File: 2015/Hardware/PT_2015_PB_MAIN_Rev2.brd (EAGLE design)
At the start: 142.2 x 170.8 mm, 135 parts, among them Q1 Q_ACS711LC, Q11 Q_IRFS7437PbF, Q12 2N7002, Q14 Q_IRFS7437PbF, Q16 Q_IRFS7437PbF, Q18 Q_FDT86102LZ, Q20 Q_IRFS7437PbF, Q4 Q_ACS711LC, Q5 Q_ACS711LC, Q6 Q_IRFS7437PbF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

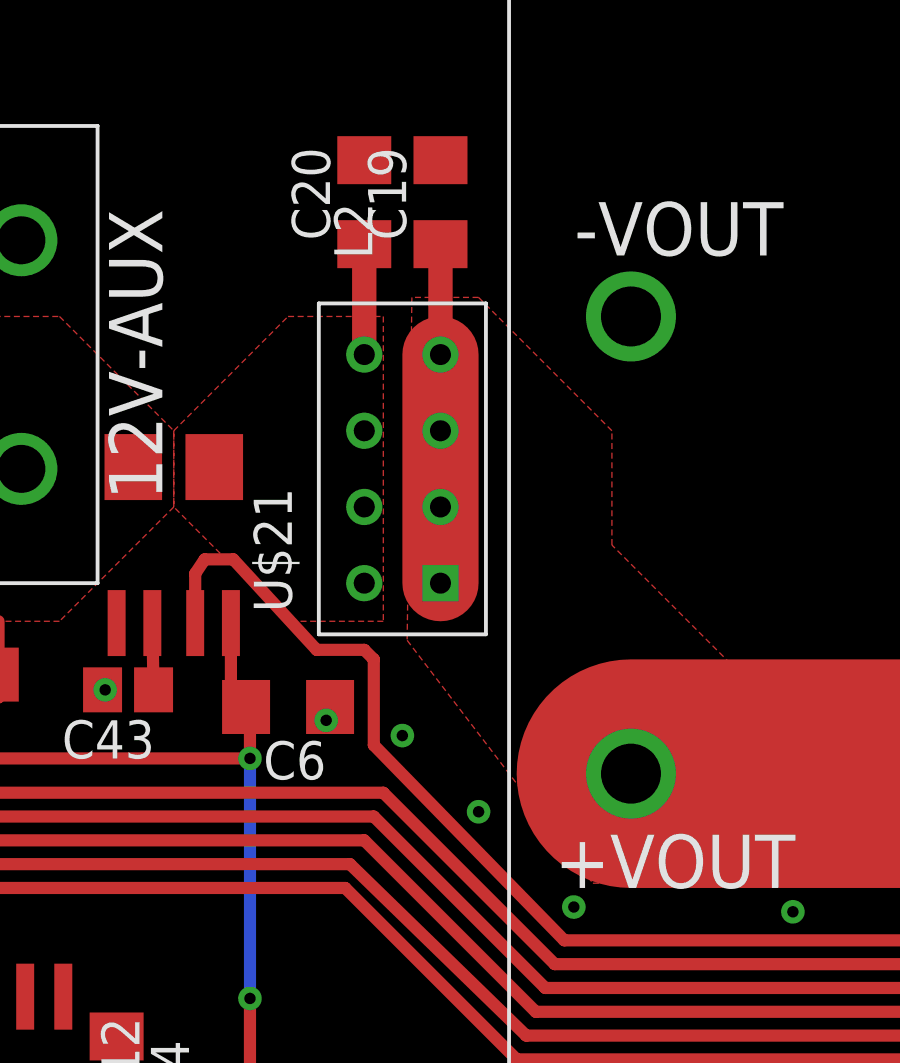
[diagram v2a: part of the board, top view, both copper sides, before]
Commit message: Removed ferrite bede on 12V non-critical output
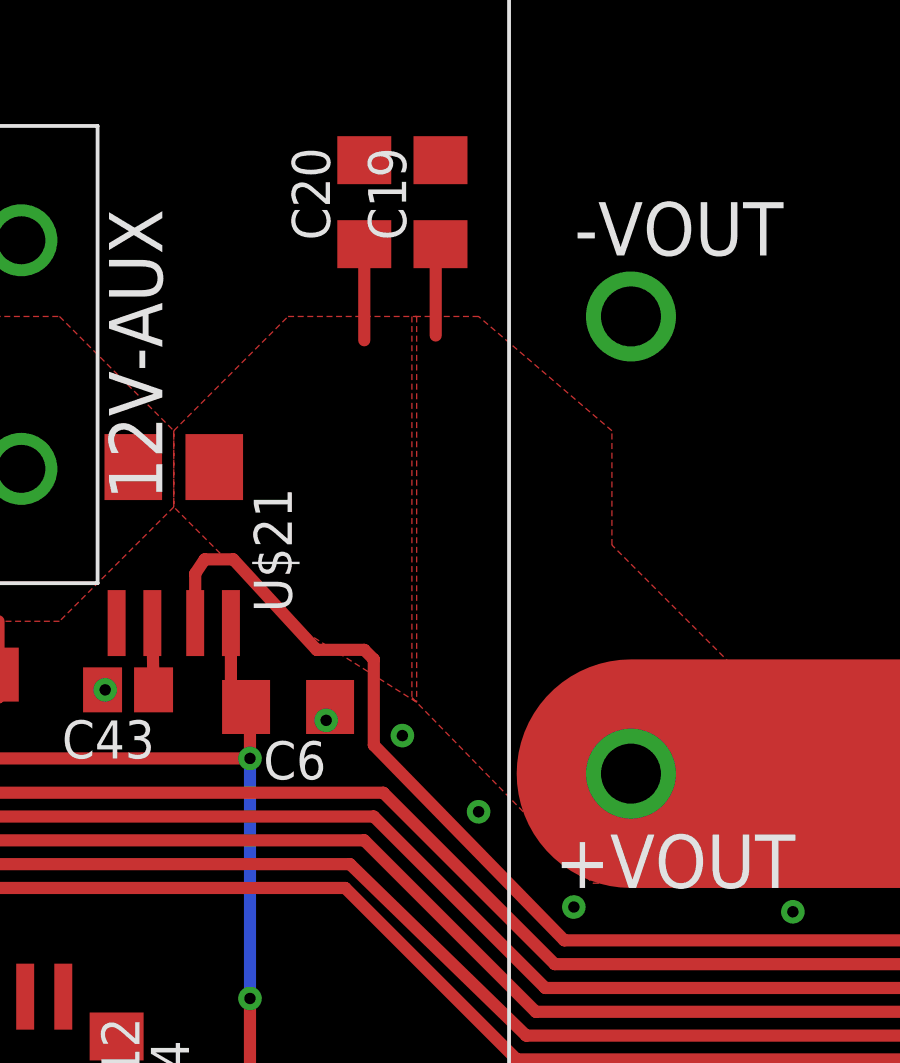
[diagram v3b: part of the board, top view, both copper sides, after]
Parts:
- removed L2: L_29F0429, MRDT-2014-All:L_29F0429
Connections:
- removed net N$11: C20.1, L2.5, L2.6, L2.7, L2.8, U$21.1
- net N$7: now also C20.1, U$21.1; no longer L2.1, L2.2, L2.3, L2.4
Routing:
- net N$7: track 88.5 -> 83.6 mm
- net N$11: track 3.68 -> 0.00 mm
- removed copper zone on layer 1, net N$11
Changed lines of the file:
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@@
 <attribute name="NAME" x="81.01" y="79.36" size="1.27" layer="25" rot="R270"/>
-</element>
-<element name="L2" library="MRDT-2014-All" package="L_29F0429" value="L_29F0429" x="24.13" y="146.05" smashed="yes" rot="R90">
-<attribute name="NAME" x="23.13" y="153.05" size="1.27" layer="25" rot="R90"/>
 </element>
 <element name="U$2" library="MRDT-2014-All" package="SOD-323" value="D_SD12T1G" x="132.08" y="99.06"/>
@@
 <contactref element="PALPATINE-12V" pad="8"/>
 <contactref element="SIDEOUS-12V" pad="8"/>
-<contactref element="L2" pad="4"/>
-<contactref element="L2" pad="1"/>
-<contactref element="L2" pad="2"/>
-<contactref element="L2" pad="3"/>
 <contactref element="C19" pad="1"/>
-<wire x1="25.4" y1="149.86" x2="25.4" y2="153.54" width="0.8128" layer="1"/>
-<wire x1="25.4" y1="149.86" x2="25.4" y2="142.24" width="2.54" layer="1"/>
 <wire x1="31.75" y1="135.89" x2="57.785" y2="135.89" width="7.62" layer="1"/>
 <wire x1="57.785" y1="135.89" x2="80.01" y2="158.115" width="7.62" layer="1"/>
 <wire x1="80.01" y1="158.115" x2="99.695" y2="158.115" width="7.62" layer="1"/>
 <polygon width="0.4064" layer="1">
-<vertex x="26.67" y="151.765"/>
-<vertex x="24.4475" y="151.765"/>
-<vertex x="24.28875" y="140.335"/>
+<vertex x="26.67" y="151.13"/>
+<vertex x="24.4475" y="151.13"/>
+<vertex x="24.4475" y="138.43"/>
 <vertex x="30.48" y="132.23875"/>
 <vertex x="36.195" y="132.23875"/>
@@
 <vertex x="31.115" y="147.32"/>
 </polygon>
-</signal>
-<signal name="N$11">
-<contactref element="L2" pad="8"/>
-<contactref element="L2" pad="5"/>
-<contactref element="L2" pad="7"/>
-<contactref element="L2" pad="6"/>
 <contactref element="C20" pad="1"/>
 <contactref element="U$21" pad="1"/>
 <polygon width="0.4064" layer="1" thermals="no">
-<vertex x="23.495" y="151.13"/>
-<vertex x="23.495" y="140.97"/>
+<vertex x="24.60625" y="151.13"/>
+<vertex x="24.60625" y="138.27125"/>
 <vertex x="20.32" y="140.97"/>
 <vertex x="16.51" y="144.78"/>
@@
 <vertex x="20.32" y="151.13"/>
 </polygon>
-<wire x1="22.86" y1="153.54" x2="22.86" y2="149.86" width="0.8128" layer="1"/>
+<wire x1="22.86" y1="153.54" x2="22.86" y2="150.33625" width="0.4064" layer="1"/>
+<wire x1="25.4" y1="153.54" x2="25.24125" y2="153.54" width="0.4064" layer="1"/>
+<wire x1="25.24125" y1="153.54" x2="25.24125" y2="150.495" width="0.4064" layer="1"/>
 </signal>
 <signal name="12V-IMEAS">

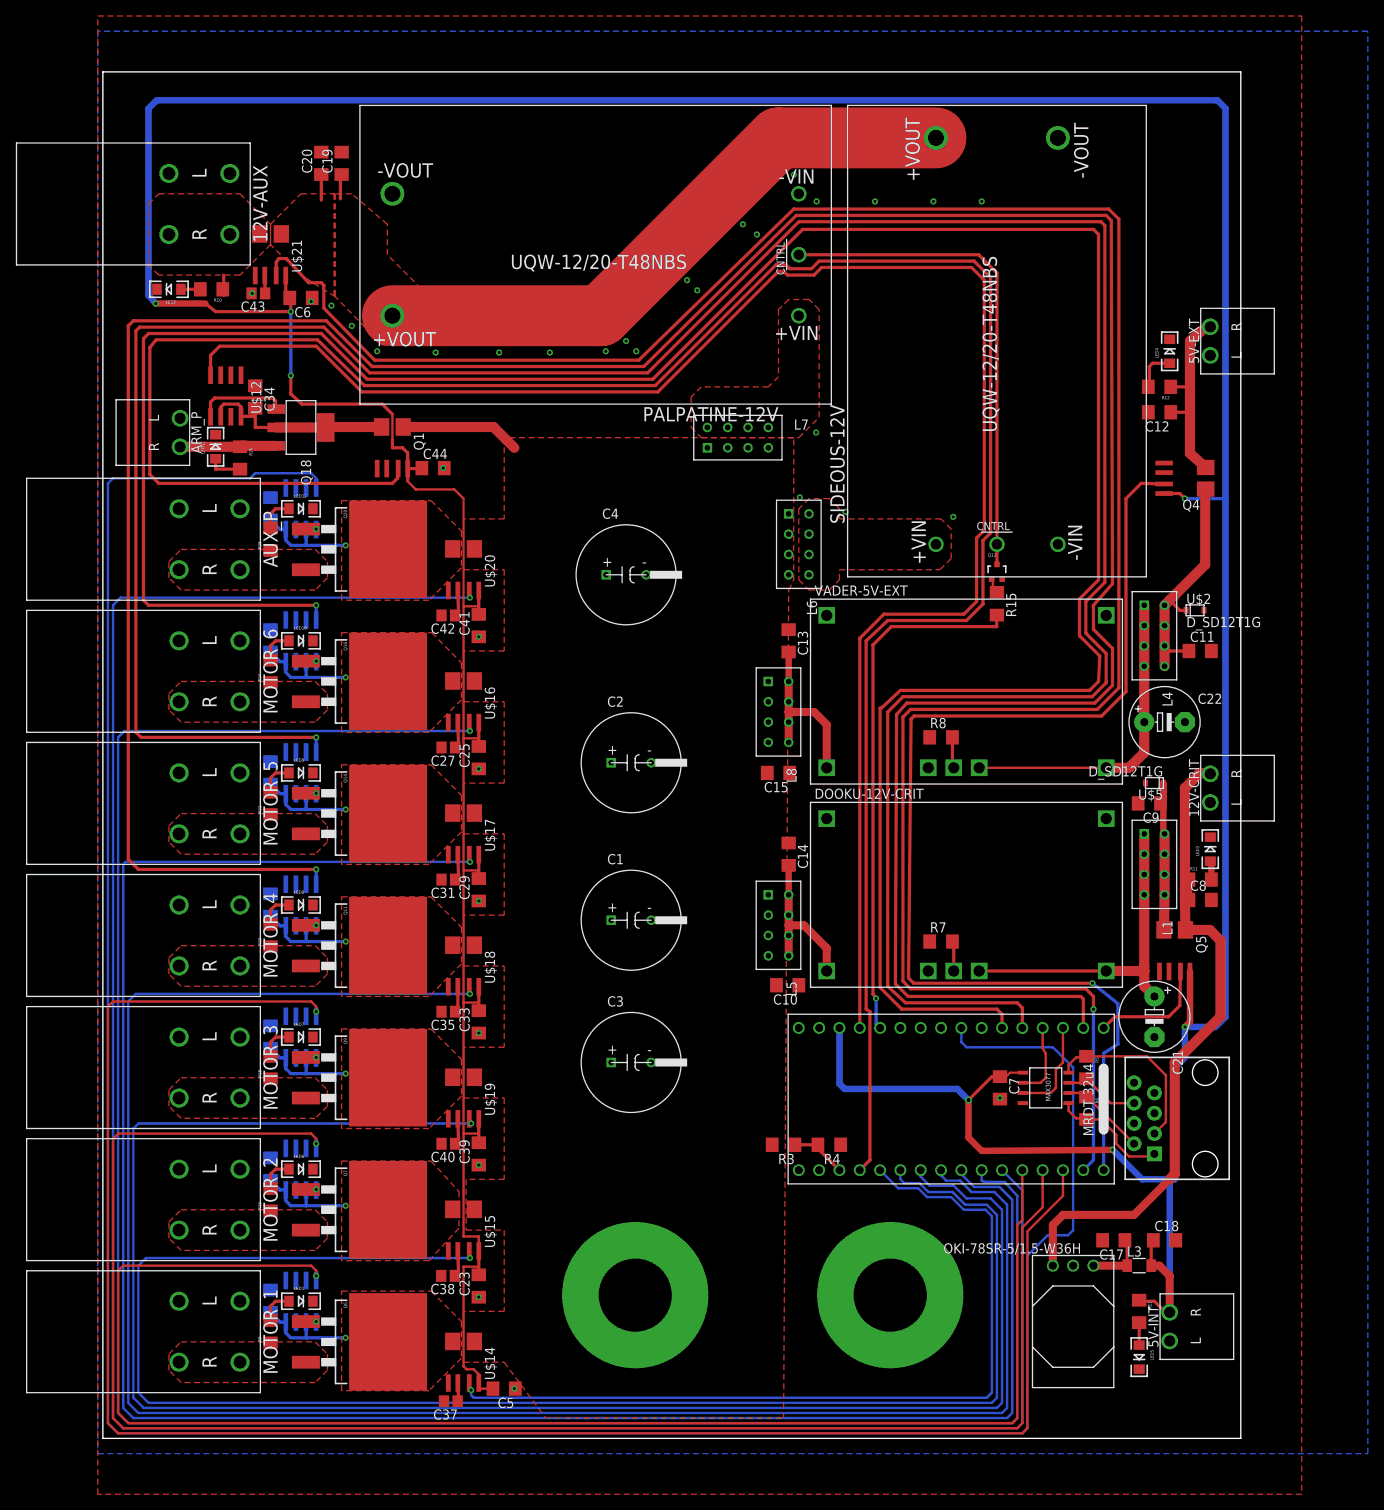
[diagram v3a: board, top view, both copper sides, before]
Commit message: Replaced input ferrites and output caps on 12V NC
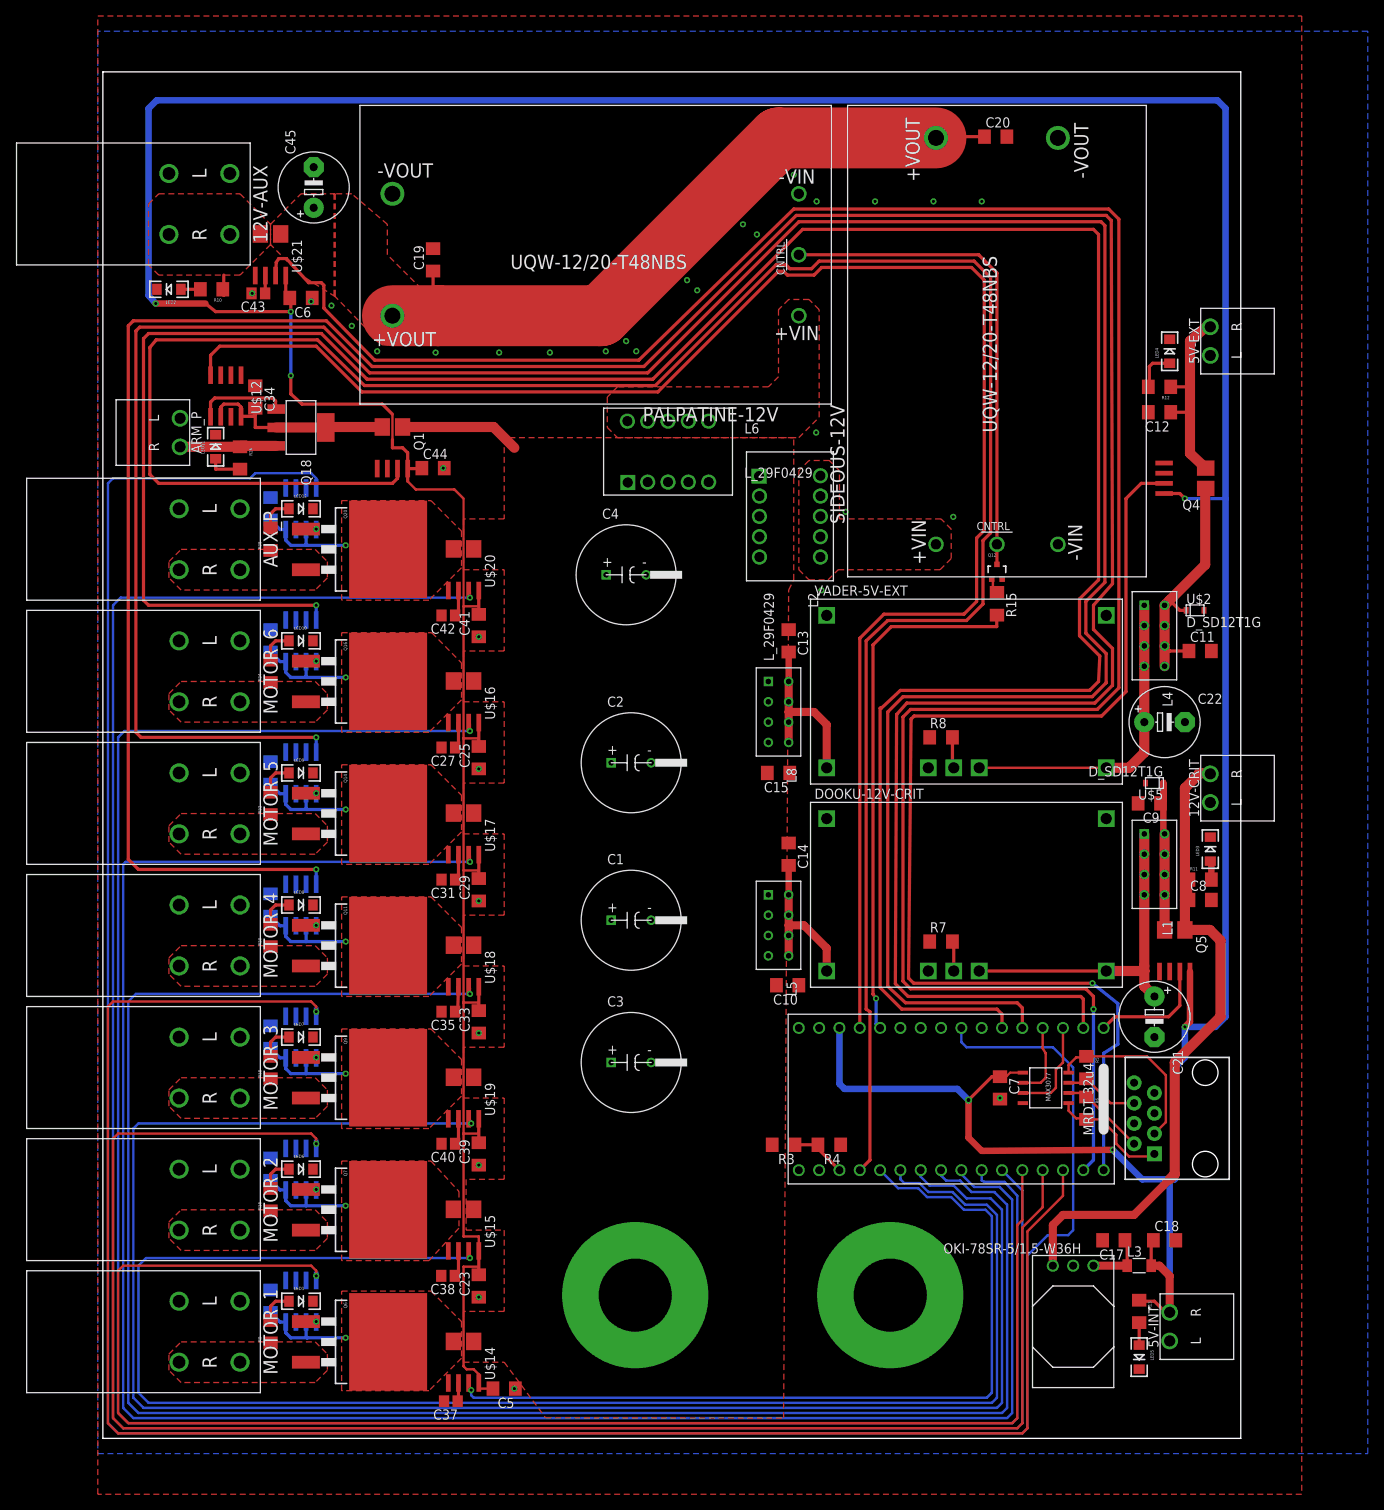
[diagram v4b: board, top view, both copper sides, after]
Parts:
- removed L7: L_29F0429, MRDT-2014-All:L_29F0429
- added C45: 330µF, resistor:E5-8,5
- added L2: L_29F0429, MRDT-2015-PowerBoard:L_29F0528
- L6: device MRDT-2014-All:L_29F0429 -> MRDT-2015-PowerBoard:L_29F0528
- moved C20 84.4 mm to (107.2, 158.3), turned to 0 degrees
- moved L6 22.5 mm to (66.2, 122.7), turned to 0 degrees
- moved C19 16.6 mm to (36.8, 142.9)
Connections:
- net GND: now also C45.-
- net N$5: now also L6.10, L6.6, L6.7, L6.8; no longer L7.5, L7.6, L7.7, L7.8
- net N$6: now also L2.10, L2.6, L2.7, L2.8, L2.9; no longer L6.5, L6.6, L6.7, L6.8
- net N$7: now also C45.+
- net V_BATT: now also L2.1, L2.2, L2.3, L2.4, L2.5, L6.5; no longer L7.1, L7.2, L7.3, L7.4
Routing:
- net N$7: track 83.6 -> 90.5 mm

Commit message: Added TVS diodes and minor trace adjustments
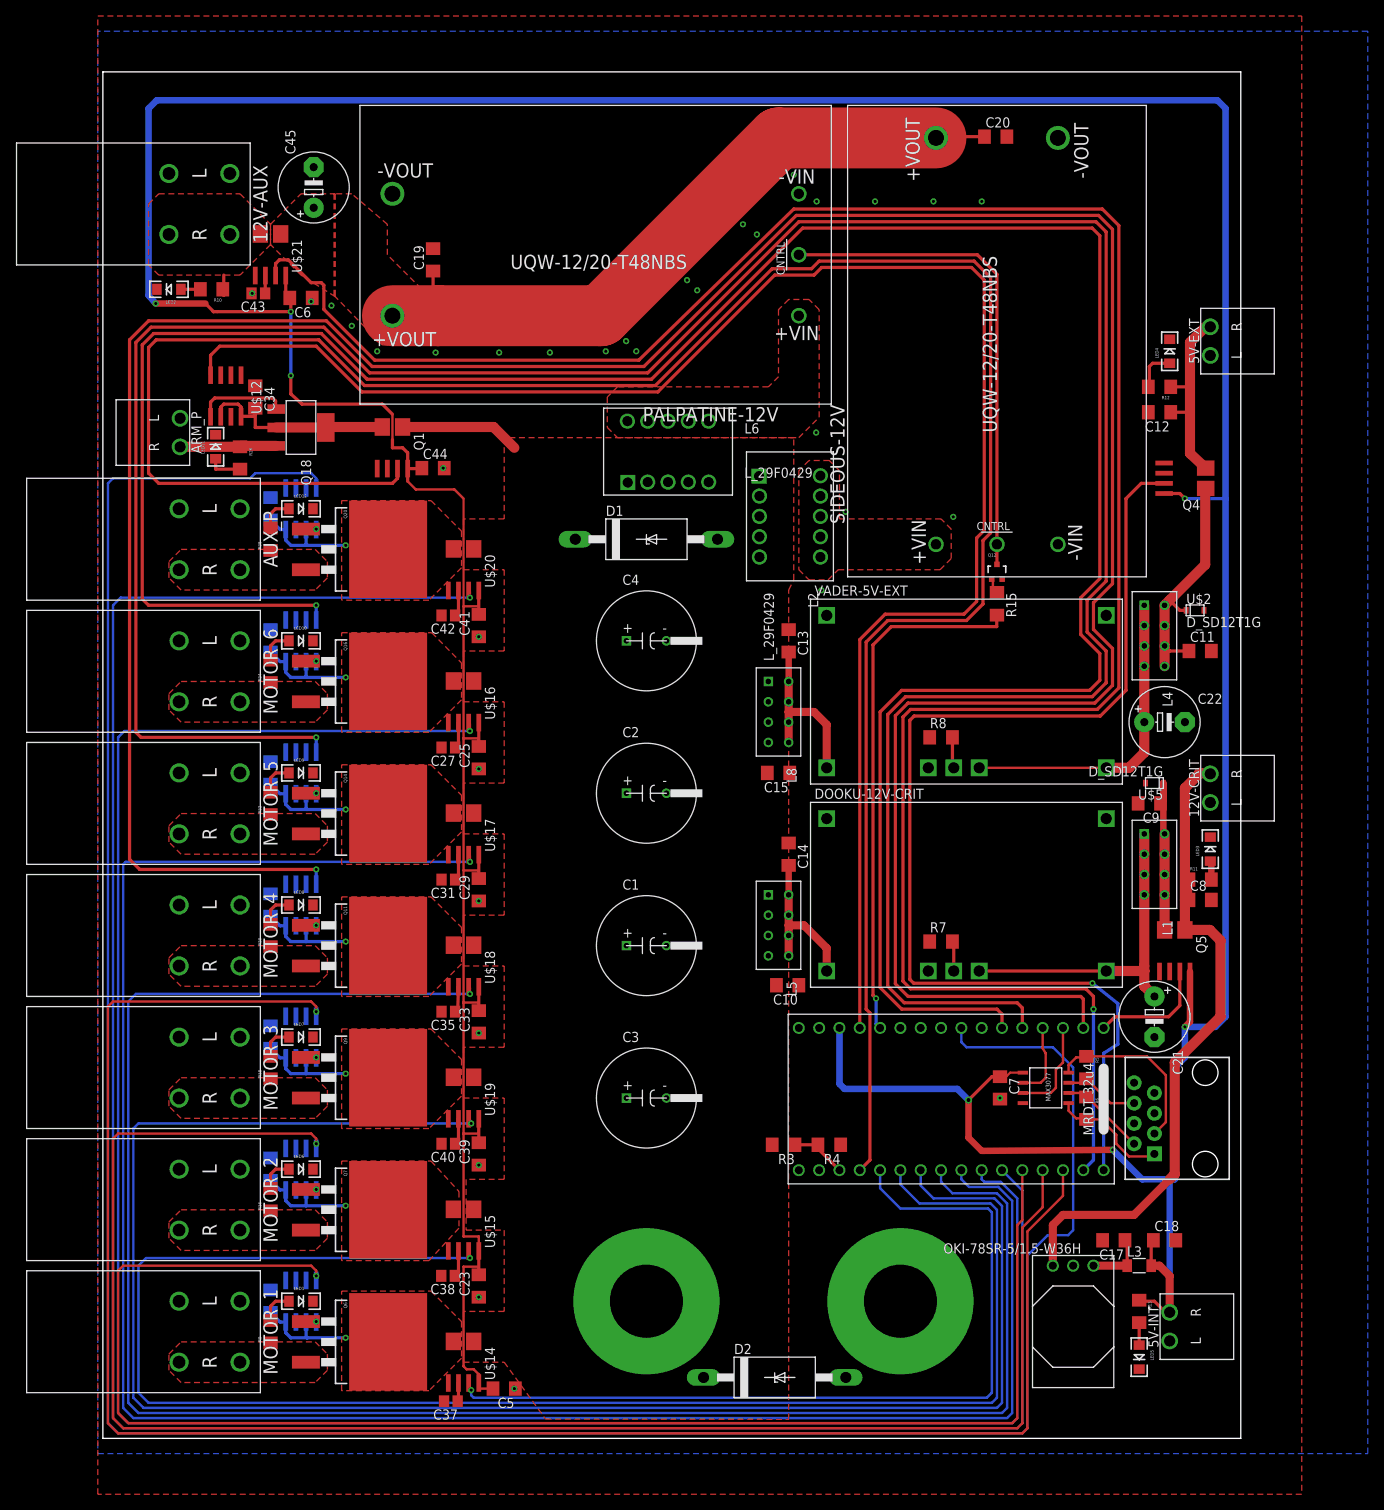
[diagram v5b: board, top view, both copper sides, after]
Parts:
- added D1, D2: 1.5KE36A, diode:CB429-17
- moved C4 8.64 mm to (63.5, 95.2)
- moved C3 4.84 mm to (63.5, 38.1)
- moved C2 4.26 mm to (63.5, 76.2)
- moved C1 3.70 mm to (63.5, 57.1)
- moved BATT-POS 1.59 mm to (63.5, 12.7)
- moved BATT-NEG 1.48 mm to (95.2, 12.7)
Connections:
- net GND: now also D1.A, D2.A
- net V_BATT: now also D1.C, D2.C
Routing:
- net M4-SIG: track 376.2 -> 374.5 mm
- net M1-IMEAS: track 105.6 -> 107.2 mm
- net M5-SIG: track 349.2 -> 347.9 mm
- net M3-IMEAS: track 223.1 -> 224.0 mm
- net M2-IMEAS: track 204.7 -> 205.4 mm
- net 12V-IMEAS: track 289.4 -> 288.7 mm
- net M4-IMEAS: track 240.7 -> 241.3 mm
